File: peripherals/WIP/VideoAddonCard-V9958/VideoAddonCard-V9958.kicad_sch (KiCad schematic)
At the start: 24 parts, among them J1 VideoAddon, U1 41464, U2 41464, U3 41464, U4 41464, U5 41464, U6 41464, U7 V9958, U8 74LS32, X1 Crystal_Generic

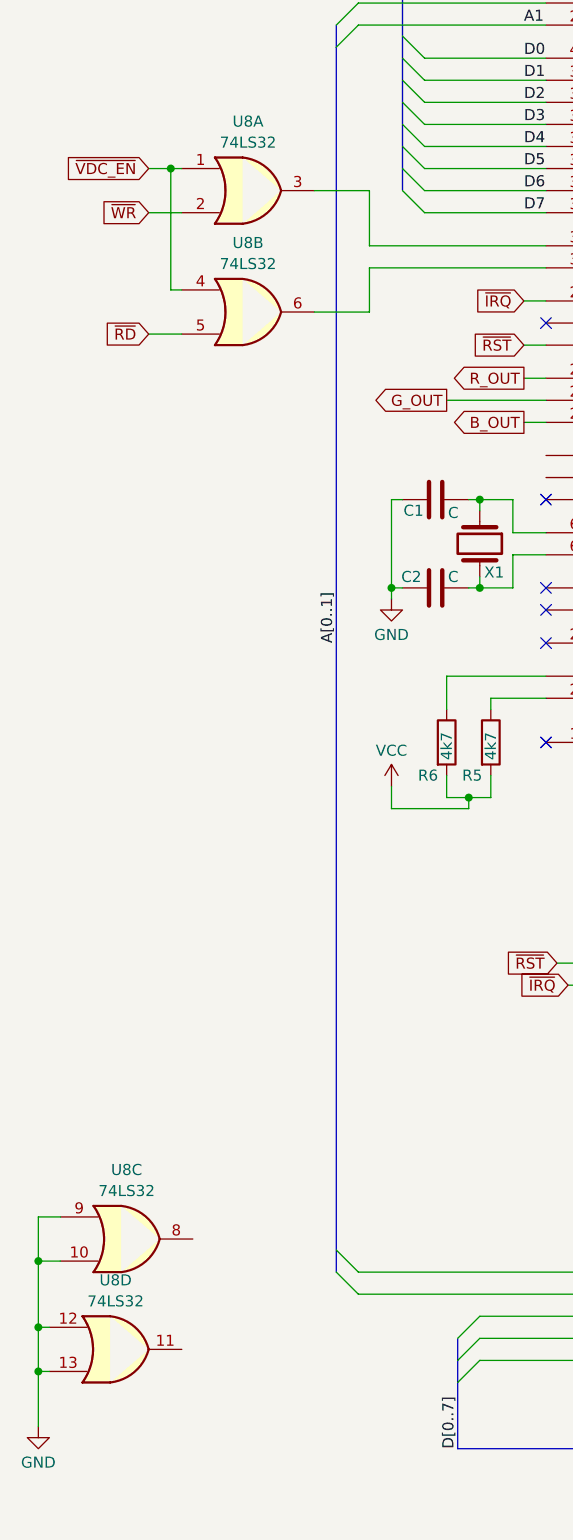
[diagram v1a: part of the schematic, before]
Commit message: Updated stage 3 with ps2 fix, added warning to PS/2 proto
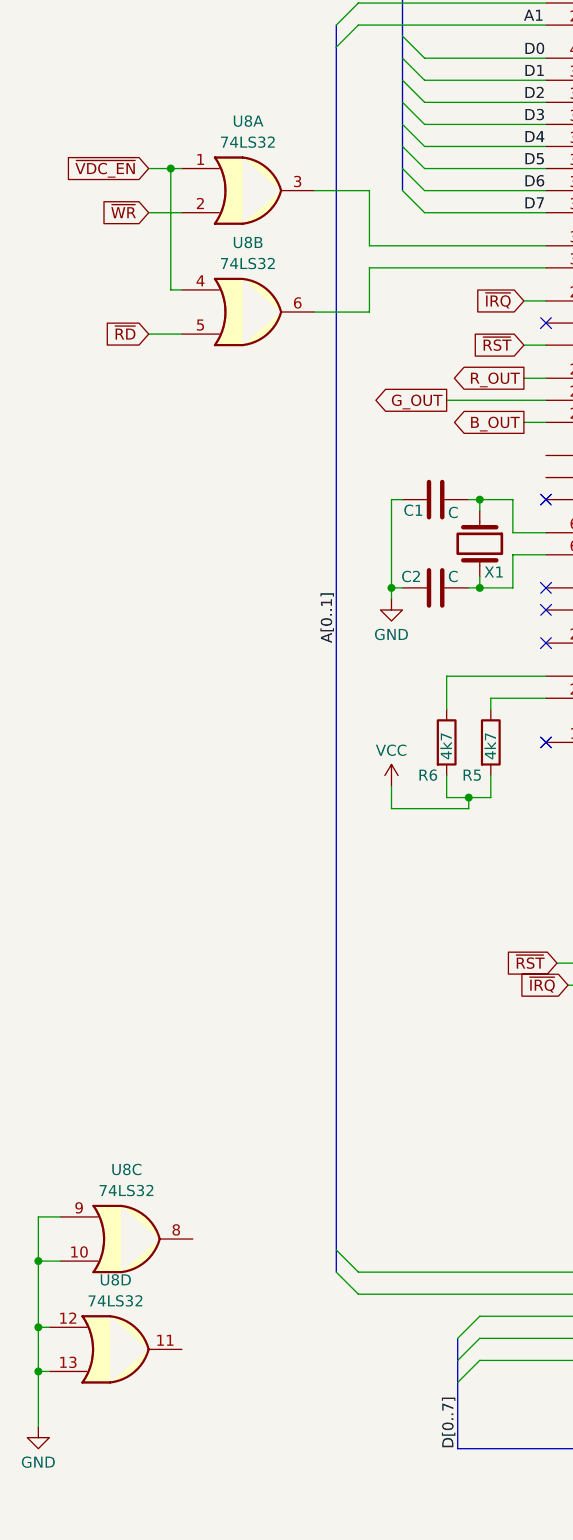
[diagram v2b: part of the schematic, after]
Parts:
- C1, C2, C3, C4, C5, C6: footprint (none) -> Capacitor_THT:C_Axial_L3.8mm_D2.6mm_P7.50mm_Horizontal
- R1, R2, R3, R4, R5, R6, R7: footprint (none) -> Resistor_THT:R_Axial_DIN0411_L9.9mm_D3.6mm_P5.08mm_Vertical
- U1, U2, U3, U4, U5, U6, U9: footprint (none) -> Package_DIP:DIP-18_W7.62mm_Socket
- U7: footprint (none) -> Package_DIP:DIP-64_W22.86mm_Socket
- U8: footprint (none) -> Package_DIP:DIP-14_W7.62mm_Socket
- X1: footprint (none) -> Crystal:Crystal_HC49-4H_Vertical
